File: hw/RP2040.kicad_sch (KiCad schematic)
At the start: 26 parts, among them J3 USB_BOOT, U5 W25Q128JVSIM, U6 RP2040, Y1 12M

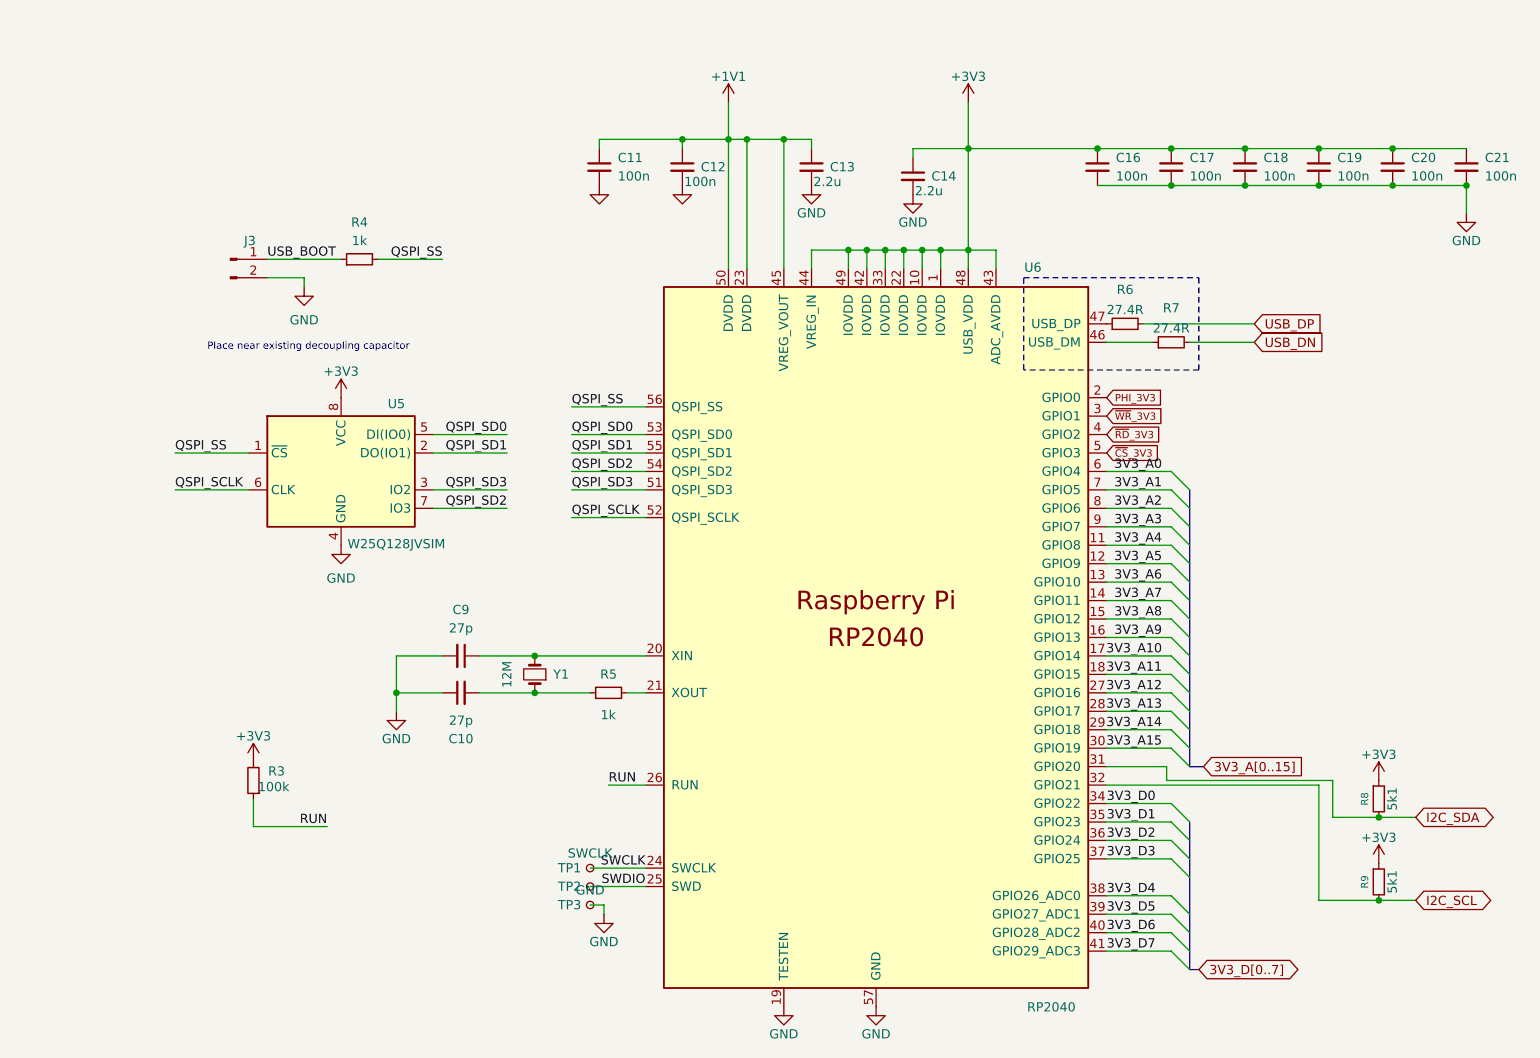
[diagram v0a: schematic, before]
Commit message: Complete layout and start placing tracks
Signed-off-by: Mahyar Koshkouei <mk@deltabeard.com>
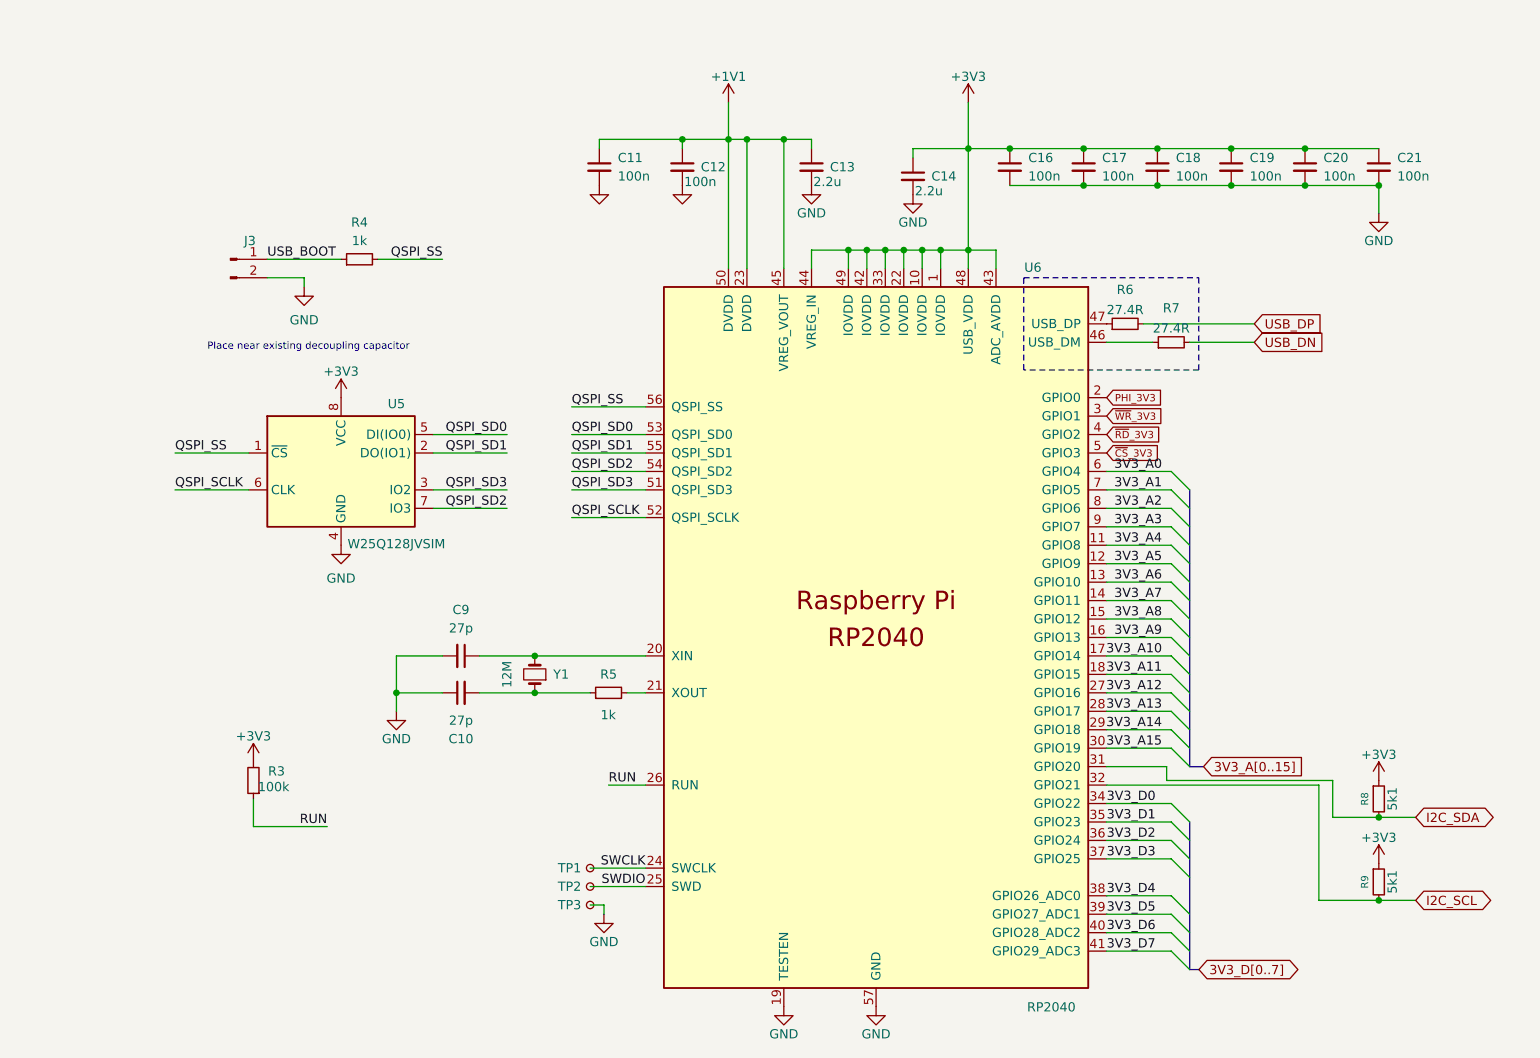
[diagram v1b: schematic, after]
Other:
- moved on the sheet: C16, C17, C18, C19, C20, C21

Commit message: hw: use parts from LCSC
Signed-off-by: Mahyar Koshkouei <mk@deltabeard.com>
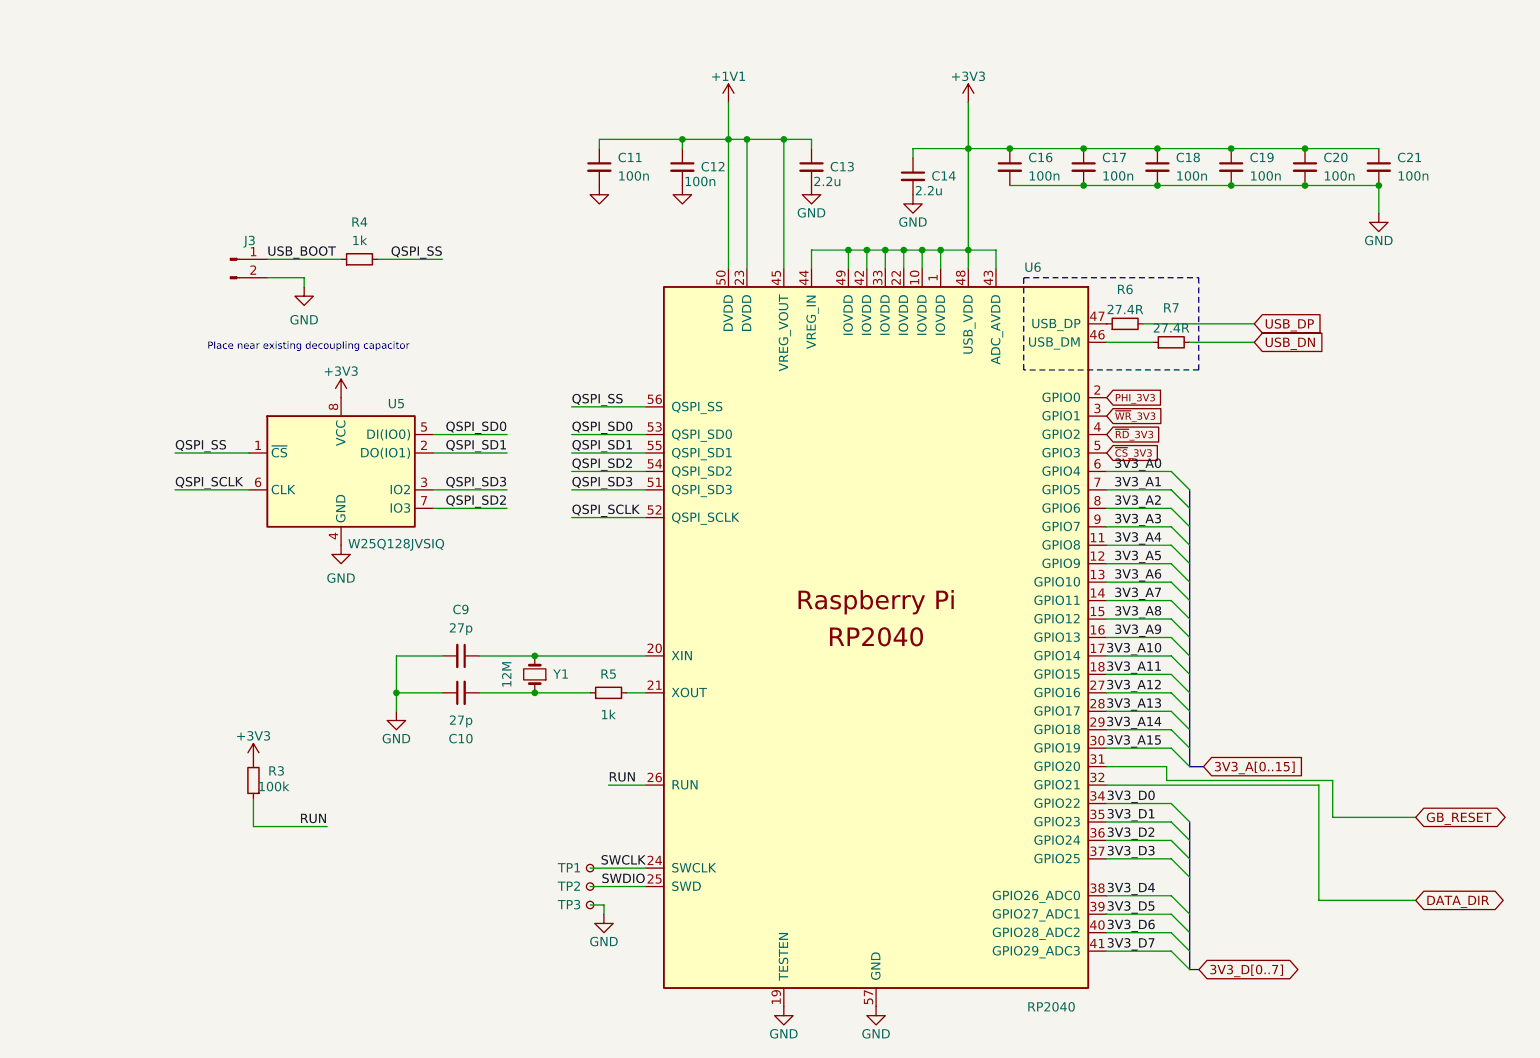
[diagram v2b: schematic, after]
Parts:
- removed R8, R9: 5k1, Resistor_SMD:R_0603_1608Metric, symbol Device:R_Small
- U5: value W25Q128JVSIM -> W25Q128JVSIQ; LCSC (none) -> C97521
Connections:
- net I2C_SCL renamed DATA_DIR
- net I2C_SDA renamed GB_RESET
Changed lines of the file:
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@@
   (junction (at 210.185 39.37) (diameter 0.9144) (color 0 0 0 0))
   (junction (at 220.345 39.37) (diameter 0.9144) (color 0 0 0 0))
-  (junction (at 220.345 126.365) (diameter 0.9144) (color 0 0 0 0))
-  (junction (at 220.345 137.795) (diameter 0.9144) (color 0 0 0 0))
   (bus_entry (at 191.77 78.74) (size 2.54 2.54)
     (stroke (width 0) (type solid) (color 0 0 0 0))
@@
     (stroke (width 0) (type solid) (color 0 0 0 0))
   )
-  (wire (pts (xy 212.09 137.795) (xy 220.345 137.795))
+  (wire (pts (xy 212.09 137.795) (xy 225.425 137.795))
     (stroke (width 0) (type solid) (color 0 0 0 0))
   )
@@
     (stroke (width 0) (type solid) (color 0 0 0 0))
   )
-  (wire (pts (xy 213.995 126.365) (xy 220.345 126.365))
+  (wire (pts (xy 213.995 126.365) (xy 225.425 126.365))
     (stroke (width 0) (type solid) (color 0 0 0 0))
   )
   (wire (pts (xy 220.345 39.37) (xy 220.345 43.18))
-    (stroke (width 0) (type solid) (color 0 0 0 0))
-  )
-  (wire (pts (xy 220.345 126.365) (xy 225.425 126.365))
-    (stroke (width 0) (type solid) (color 0 0 0 0))
-  )
-  (wire (pts (xy 220.345 137.795) (xy 225.425 137.795))
     (stroke (width 0) (type solid) (color 0 0 0 0))
   )
@@
     )
   )
-  (global_label "I2C_SDA" (shape bidirectional) (at 225.425 126.365 0) (fields_autoplaced)
+  (global_label "GB_RESET" (shape bidirectional) (at 225.425 126.365 0) (fields_autoplaced)
     (effects (font (size 1.27 1.27)) (justify left))
-    (property "Intersheet References" "${INTERSHEET_REFS}" (id 0) (at 235.3628 126.2856 0)
+    (property "Intersheet References" "${INTERSHEET_REFS}" (id 0) (at 236.9957 126.2856 0)
       (effects (font (size 1.27 1.27)) (justify left) hide)
     )
   )
-  (global_label "I2C_SCL" (shape bidirectional) (at 225.425 137.795 0) (fields_autoplaced)
+  (global_label "DATA_DIR" (shape bidirectional) (at 225.425 137.795 0) (fields_autoplaced)
     (effects (font (size 1.27 1.27)) (justify left))
-    (property "Intersheet References" "${INTERSHEET_REFS}" (id 0) (at 235.3023 137.7156 0)
+    (property "Intersheet References" "${INTERSHEET_REFS}" (id 0) (at 236.2699 137.7156 0)
       (effects (font (size 1.27 1.27)) (justify left) hide)
     )
@@
     )
     (property "Datasheet" "" (id 3) (at 163.83 27.94 0)
-      (effects (font (size 1.27 1.27)) hide)
-    )
-    (pin "1")
-  )
-  (symbol (lib_id "power:+3V3") (at 220.345 121.285 0) (unit 1)
-    (in_bom yes) (on_board yes) (fields_autoplaced)
-    (property "Reference" "#PWR046" (id 0) (at 220.345 125.095 0)
-      (effects (font (size 1.27 1.27)) hide)
-    )
-    (property "Value" "+3V3" (id 1) (at 220.345 117.729 0))
-    (property "Footprint" "" (id 2) (at 220.345 121.285 0)
-      (effects (font (size 1.27 1.27)) hide)
-    )
-    (property "Datasheet" "" (id 3) (at 220.345 121.285 0)
-      (effects (font (size 1.27 1.27)) hide)
-    )
-    (pin "1")
-  )
-  (symbol (lib_id "power:+3V3") (at 220.345 132.715 0) (unit 1)
-    (in_bom yes) (on_board yes) (fields_autoplaced)
-    (property "Reference" "#PWR047" (id 0) (at 220.345 136.525 0)
-      (effects (font (size 1.27 1.27)) hide)
-    )
-    (property "Value" "+3V3" (id 1) (at 220.345 129.159 0))
-    (property "Footprint" "" (id 2) (at 220.345 132.715 0)
-      (effects (font (size 1.27 1.27)) hide)
-    )
-    (property "Datasheet" "" (id 3) (at 220.345 132.715 0)
       (effects (font (size 1.27 1.27)) hide)
     )
@@
     (pin "2")
   )
-  (symbol (lib_id "Device:R_Small") (at 220.345 123.825 0) (unit 1)
-    (in_bom yes) (on_board yes)
-    (property "Reference" "R8" (id 0) (at 218.4168 123.825 90)
-      (effects (font (size 1 1)))
-    )
-    (property "Value" "5k1" (id 1) (at 222.2269 123.825 90))
-    (property "Footprint" "Resistor_SMD:R_0603_1608Metric" (id 2) (at 220.345 123.825 0)
-      (effects (font (size 1.27 1.27)) hide)
-    )
-    (property "Datasheet" "~" (id 3) (at 220.345 123.825 0)
-      (effects (font (size 1.27 1.27)) hide)
-    )
-    (pin "1")
-    (pin "2")
-  )
-  (symbol (lib_id "Device:R_Small") (at 220.345 135.255 0) (unit 1)
-    (in_bom yes) (on_board yes)
-    (property "Reference" "R9" (id 0) (at 218.4168 135.255 90)
-      (effects (font (size 1 1)))
-    )
-    (property "Value" "5k1" (id 1) (at 222.2269 135.255 90))
-    (property "Footprint" "Resistor_SMD:R_0603_1608Metric" (id 2) (at 220.345 135.255 0)
-      (effects (font (size 1.27 1.27)) hide)
-    )
-    (property "Datasheet" "~" (id 3) (at 220.345 135.255 0)
-      (effects (font (size 1.27 1.27)) hide)
-    )
-    (pin "1")
-    (pin "2")
-  )
   (symbol (lib_id "Device:Crystal_Small") (at 104.14 106.68 90) (unit 1)
     (in_bom yes) (on_board yes)
@@
     (in_bom yes) (on_board yes)
     (property "Reference" "U5" (id 0) (at 85.09 69.4394 0))
-    (property "Value" "W25Q128JVSIM" (id 1) (at 85.09 88.7245 0))
+    (property "Value" "W25Q128JVSIQ" (id 1) (at 85.09 88.7245 0))
     (property "Footprint" "Package_SO:SOIC-8_5.23x5.23mm_P1.27mm" (id 2) (at 77.47 78.74 0)
       (effects (font (size 1.27 1.27)) hide)
@@
       (effects (font (size 1.27 1.27)) hide)
     )
+    (property "LCSC" "C97521" (id 4) (at 77.47 78.74 0)
+      (effects (font (size 1.27 1.27)) hide)
+    )

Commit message: hw: complete 2-layer PCB
Signed-off-by: Mahyar Koshkouei <mk@deltabeard.com>
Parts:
- removed J3: USB_BOOT, Button_Switch_THT:SW_PUSH_6mm, symbol Connector:Conn_01x02_Male
- removed Y1: 12M, Crystal:Crystal_SMD_TXC_7A-2Pin_5x3.2mm, symbol Device:Crystal_Small
- added C26: 100n, Capacitor_SMD:C_0402_1005Metric, symbol Device:C_Small
- added C27: 2.2u, Capacitor_SMD:C_0603_1608Metric, symbol Device:C_Small
- added TP2, TP3, TP4, TP5: TestPoint, TestPoint:TestPoint_Pad_D1.5mm, symbol Connector:TestPoint
- added Y1: Crystal_GND24, Crystal:Crystal_SMD_3225-4Pin_3.2x2.5mm, symbol Device:Crystal_GND24
- C10, C9: value 27p -> 30p; LCSC (none) -> C22397
- C11, C12: footprint Capacitor_SMD:C_0603_1608Metric -> Capacitor_SMD:C_0402_1005Metric; LCSC (none) -> C1525
- C13, C14: LCSC (none) -> C23630
- C15: renamed from C16; footprint Capacitor_SMD:C_0603_1608Metric -> Capacitor_SMD:C_0402_1005Metric; LCSC (none) -> C1525
- C16: renamed from C17; footprint Capacitor_SMD:C_0603_1608Metric -> Capacitor_SMD:C_0402_1005Metric; LCSC (none) -> C1525
- C17: renamed from C18; footprint Capacitor_SMD:C_0603_1608Metric -> Capacitor_SMD:C_0402_1005Metric; LCSC (none) -> C1525
- C18: renamed from C19; footprint Capacitor_SMD:C_0603_1608Metric -> Capacitor_SMD:C_0402_1005Metric; LCSC (none) -> C1525
- C19: renamed from C20; footprint Capacitor_SMD:C_0603_1608Metric -> Capacitor_SMD:C_0402_1005Metric; LCSC (none) -> C1525
- C20: renamed from C21; footprint Capacitor_SMD:C_0603_1608Metric -> Capacitor_SMD:C_0402_1005Metric; LCSC (none) -> C1525
- R3: LCSC (none) -> C25803
- R4, R5: LCSC (none) -> C21190
- R6, R7: LCSC (none) -> C25190
- U6: LCSC (none) -> C2040
- renumbered TP1 to TP6, TP2 to TP7, TP3 to TP8
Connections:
- net GB_RESET is gone; now on net 3V3_A15: U6.31 (GPIO20)
- net +1V1: now also TP4.1
- net +3V3: now also C26.1, C27.1, TP5.1
- net 3V3_A0: now also U6.7 (GPIO5); no longer U6.6 (GPIO4)
- net 3V3_A1: now also U6.8 (GPIO6); no longer U6.7 (GPIO5)
- net 3V3_A10: now also U6.18 (GPIO15); no longer U6.17 (GPIO14)
- net 3V3_A11: now also U6.27 (GPIO16); no longer U6.18 (GPIO15)
- net 3V3_A12: now also U6.28 (GPIO17); no longer U6.27 (GPIO16)
- net 3V3_A13: now also U6.29 (GPIO18); no longer U6.28 (GPIO17)
- net 3V3_A14: now also U6.30 (GPIO19); no longer U6.29 (GPIO18)
- net 3V3_A15: no longer U6.30 (GPIO19)
- net 3V3_A2: now also U6.9 (GPIO7); no longer U6.8 (GPIO6)
- net 3V3_A3: now also U6.11 (GPIO8); no longer U6.9 (GPIO7)
- net 3V3_A4: now also U6.12 (GPIO9); no longer U6.11 (GPIO8)
- net 3V3_A5: now also U6.13 (GPIO10); no longer U6.12 (GPIO9)
- net 3V3_A6: now also U6.14 (GPIO11); no longer U6.13 (GPIO10)
- net 3V3_A7: now also U6.15 (GPIO12); no longer U6.14 (GPIO11)
- net 3V3_A8: now also U6.16 (GPIO13); no longer U6.15 (GPIO12)
- net 3V3_A9: now also U6.17 (GPIO14); no longer U6.16 (GPIO13)
- net 3V3_D0: now also U6.32 (GPIO21); no longer U6.34 (GPIO22)
- net 3V3_D1: now also U6.34 (GPIO22); no longer U6.35 (GPIO23)
- net 3V3_D2: now also U6.35 (GPIO23); no longer U6.36 (GPIO24)
- net 3V3_D3: now also U6.36 (GPIO24); no longer U6.37 (GPIO25)
- net 3V3_D4: now also U6.37 (GPIO25); no longer U6.38 (GPIO26_ADC0)
- net 3V3_D5: now also U6.38 (GPIO26_ADC0); no longer U6.39 (GPIO27_ADC1)
- net 3V3_D6: now also U6.39 (GPIO27_ADC1); no longer U6.40 (GPIO28_ADC2)
- net 3V3_D7: now also U6.40 (GPIO28_ADC2); no longer U6.41 (GPIO29_ADC3)
- net DATA_DIR: now also U6.41 (GPIO29_ADC3); no longer U6.32 (GPIO21)
- net GND: now also C26.2, C27.2, TP3.1, Y1.2, Y1.4
- net PHI_3V3: now also U6.4 (GPIO2); no longer U6.2 (GPIO0)
- net USB_BOOT: now also TP2.1
- net ~{CS}_3V3: now also U6.6 (GPIO4); no longer U6.5 (GPIO3)
- net ~{RD}_3V3: now also U6.5 (GPIO3); no longer U6.4 (GPIO2)
- net at C9.1, U6.20 (XIN): now also Y1.3
- net at C10.2, R5.1: now also Y1.1
- net ~{WR}_3V3 renamed I^{2}C_{SCL}
- new net I^{2}C_{SDA}: U6.2 (GPIO0)
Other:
- note removed: "Place near existing decoupling capacitor"
- moved on the sheet: C10, C9, R4
